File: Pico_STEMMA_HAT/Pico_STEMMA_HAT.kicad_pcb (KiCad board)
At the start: 2 copper layers, 58 x 63 mm, 38 parts, among them J1 Conn_01x20_Socket, J2 Conn_01x20_Socket

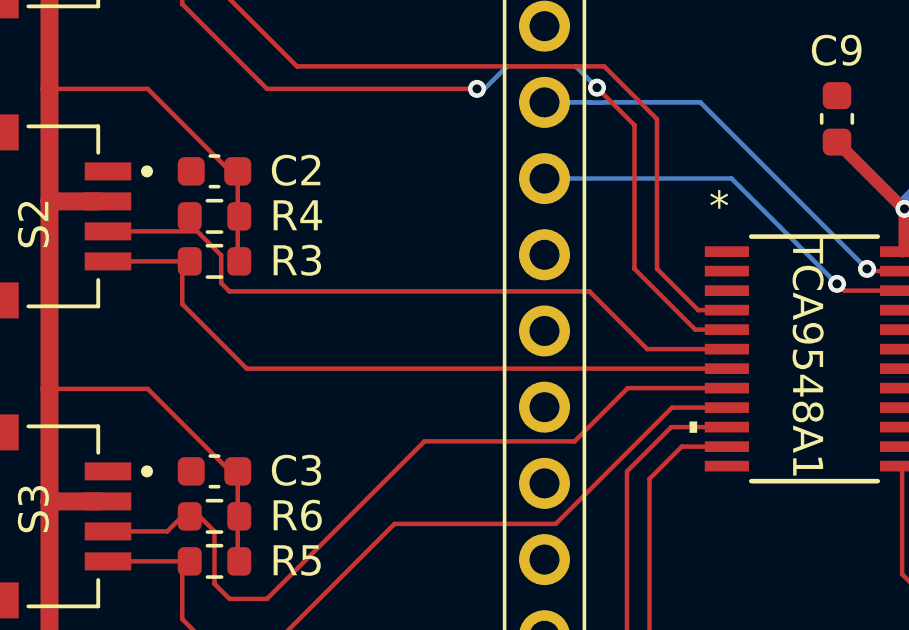
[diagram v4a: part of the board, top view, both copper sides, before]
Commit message: Reroute traces
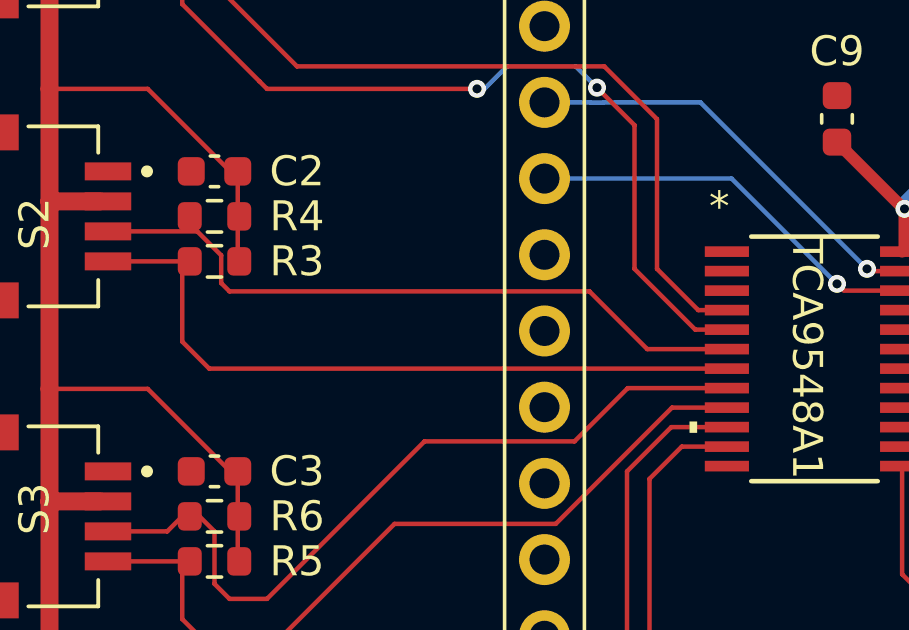
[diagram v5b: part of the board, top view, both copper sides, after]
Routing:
- net /SCL1: track 23.2 -> 23.9 mm
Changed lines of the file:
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@@
 	)
 	(segment
-		(start 131.074998 100.074998)
+		(start 128.925 99.175)
+		(end 129.824998 100.074998)
+		(width 0.15)
+		(layer "F.Cu")
+		(net 38)
+	)
+	(segment
+		(start 128.925 96.5)
+		(end 128.925 99.175)
+		(width 0.15)
+		(layer "F.Cu")
+		(net 38)
+	)
+	(segment
+		(start 129.824998 100.074998)
 		(end 147.079 100.074998)
-		(width 0.15)
-		(layer "F.Cu")
-		(net 38)
-	)
-	(segment
-		(start 128.925 96.5)
-		(end 128.925 97.925)
-		(width 0.15)
-		(layer "F.Cu")
-		(net 38)
-	)
-	(segment
-		(start 128.925 97.925)
-		(end 131.074998 100.074998)
 		(width 0.15)
 		(layer "F.Cu")
@@
 	)
 	(segment
+		(start 157.25 84.75)
+		(end 156.5 85.5)
+		(width 0.15)
+		(layer "F.Cu")
+		(net 51)
+	)
+	(segment
+		(start 156.074998 99.425002)
+		(end 152.921 99.425002)
+		(width 0.15)
+		(layer "F.Cu")
+		(net 51)
+	)
+	(segment
+		(start 174.05 84.5)
+		(end 172.75 84.5)
+		(width 0.15)
+		(layer "F.Cu")
+		(net 51)
+	)
+	(segment
+		(start 171.25 85)
+		(end 170.5 84.25)
+		(width 0.15)
+		(layer "F.Cu")
+		(net 51)
+	)
+	(segment
 		(start 156.5 85.5)
 		(end 156.5 99)
@@
 	)
 	(segment
+		(start 168.75 82)
+		(end 166 84.75)
+		(width 0.15)
+		(layer "F.Cu")
+		(net 51)
+	)
+	(segment
+		(start 170.5 82.5)
+		(end 170 82)
+		(width 0.15)
+		(layer "F.Cu")
+		(net 51)
+	)
+	(segment
+		(start 172.25 85)
+		(end 171.25 85)
+		(width 0.15)
+		(layer "F.Cu")
+		(net 51)
+	)
+	(segment
+		(start 166 84.75)
+		(end 157.25 84.75)
+		(width 0.15)
+		(layer "F.Cu")
+		(net 51)
+	)
+	(segment
+		(start 172.75 84.5)
+		(end 172.25 85)
+		(width 0.15)
+		(layer "F.Cu")
+		(net 51)
+	)
+	(segment
 		(start 170 82)
 		(end 168.75 82)
@@
 	)
 	(segment
-		(start 171.25 85)
-		(end 170.5 84.25)
-		(width 0.15)
-		(layer "F.Cu")
-		(net 51)
-	)
-	(segment
 		(start 170.5 84.25)
 		(end 170.5 82.5)
 		(width 0.15)
 		(layer "F.Cu")
-		(net 51)
-	)
-	(segment
-		(start 172.25 85)
-		(end 171.25 85)
-		(width 0.15)
-		(layer "F.Cu")
-		(net 51)
-	)
-	(segment
-		(start 172.75 84.5)
-		(end 172.25 85)
-		(width 0.15)
-		(layer "F.Cu")
-		(net 51)
-	)
-	(segment
-		(start 166 84.75)
-		(end 157.25 84.75)
-		(width 0.15)
-		(layer "F.Cu")
-		(net 51)
-	)
-	(segment
-		(start 174.05 84.5)
-		(end 172.75 84.5)
-		(width 0.15)
-		(layer "F.Cu")
-		(net 51)
-	)
-	(segment
-		(start 157.25 84.75)
-		(end 156.5 85.5)
-		(width 0.15)
-		(layer "F.Cu")
-		(net 51)
-	)
-	(segment
-		(start 170.5 82.5)
-		(end 170 82)
-		(width 0.15)
-		(layer "F.Cu")
-		(net 51)
-	)
-	(segment
-		(start 168.75 82)
-		(end 166 84.75)
-		(width 0.15)
-		(layer "F.Cu")
-		(net 51)
-	)
-	(segment
-		(start 156.074998 99.425002)
-		(end 152.921 99.425002)
-		(width 0.15)
-		(layer "F.Cu")

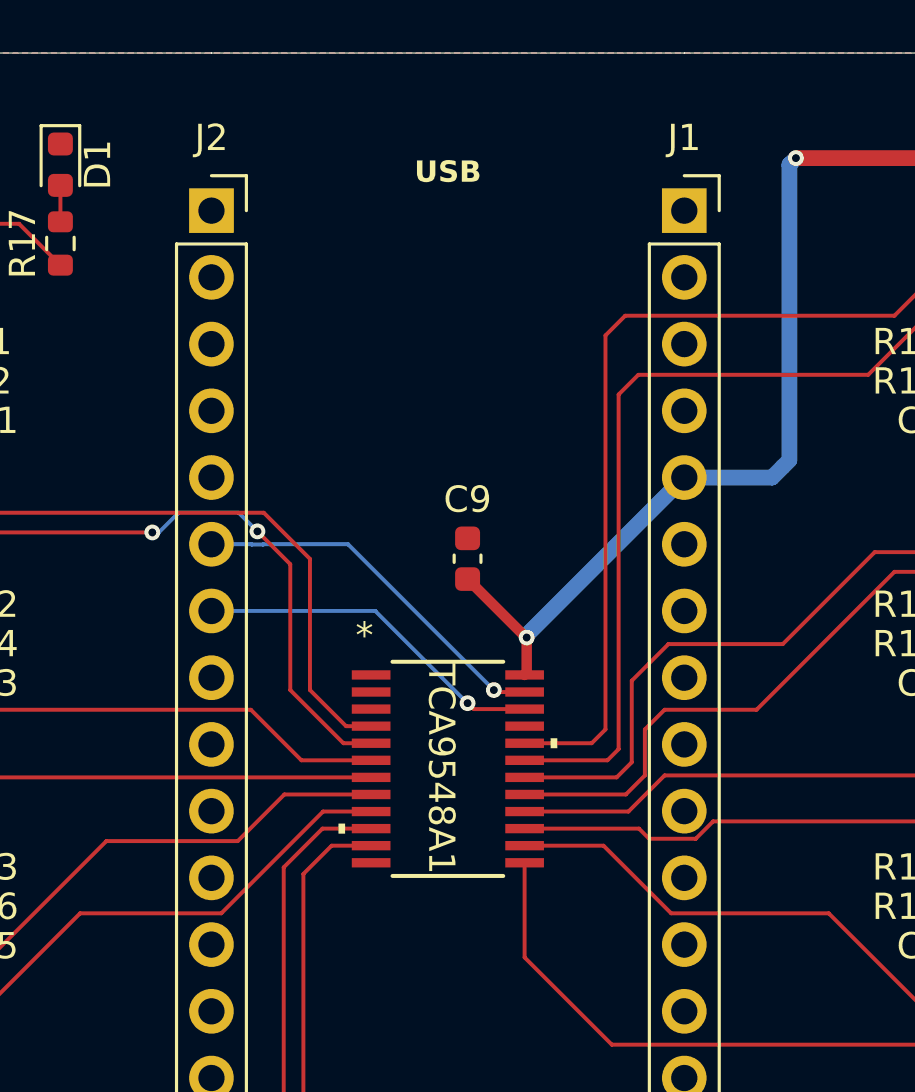
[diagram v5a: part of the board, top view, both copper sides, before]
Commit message: Add 3D models to the repo
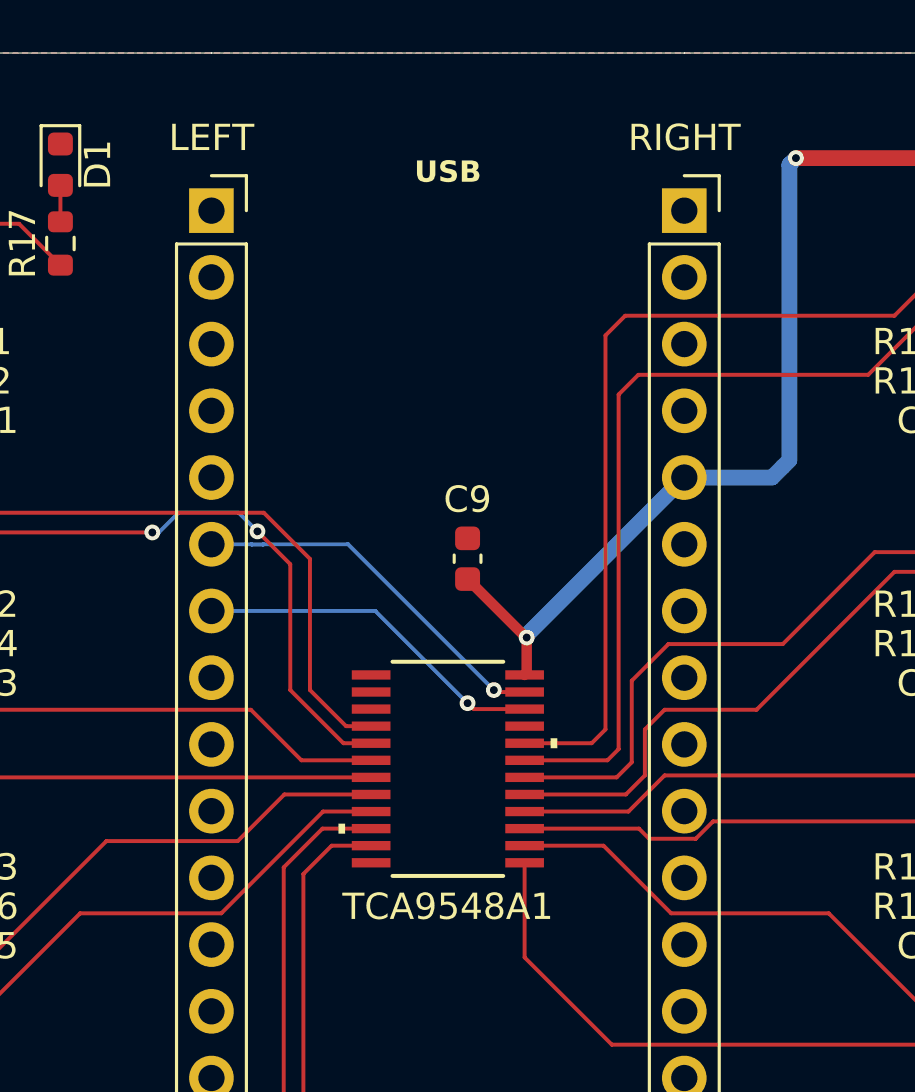
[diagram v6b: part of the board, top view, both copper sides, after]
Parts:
- renumbered J2 to LEFT, J1 to RIGHT
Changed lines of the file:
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@@
 		(descr "Through hole straight socket strip, 1x20, 2.54mm pitch, single row (from Kicad 4.0.7), script generated")
 		(tags "Through hole socket strip THT 1x20 2.54mm single row")
-		(property "Reference" "J1"
+		(property "Reference" "RIGHT"
 			(at 0 -2.77 0)
 			(layer "F.SilkS")
@@
 		(descr "Through hole straight socket strip, 1x20, 2.54mm pitch, single row (from Kicad 4.0.7), script generated")
 		(tags "Through hole socket strip THT 1x20 2.54mm single row")
-		(property "Reference" "J2"
+		(property "Reference" "LEFT"
 			(at 0 -2.77 0)
 			(layer "F.SilkS")
@@
 		(tags "TCA9548APWR ")
 		(property "Reference" "TCA9548A1"
-			(at -0.25 0 -90)
+			(at 0 5.25 0)
 			(unlocked yes)
 			(layer "F.SilkS")
@@
 			(layer "F.Fab")
 		)
-		(fp_text user "*"
-			(at -3.175 -5.0736 0)
-			(layer "F.SilkS")
-			(effects
-				(font
-					(size 1 1)
-					(thickness 0.15)
-				)
-			)
-		)
-		(fp_text user "*"
-			(at -3.175 -5.0736 0)
-			(layer "F.SilkS")
-			(effects
-				(font
-					(size 1 1)
-					(thickness 0.15)
-				)
-			)
-		)
-		(fp_text user "*"
-			(at -1.8669 -3.8735 0)
+		(fp_text user "${REFERENCE}"
+			(at 0 5.25 0)
 			(unlocked yes)
 			(layer "F.Fab")
@@
 			)
 		)
-		(fp_text user "${REFERENCE}"
-			(at 0 5.25 0)
+		(fp_text user "*"
+			(at -1.8669 -3.8735 0)
 			(unlocked yes)
 			(layer "F.Fab")

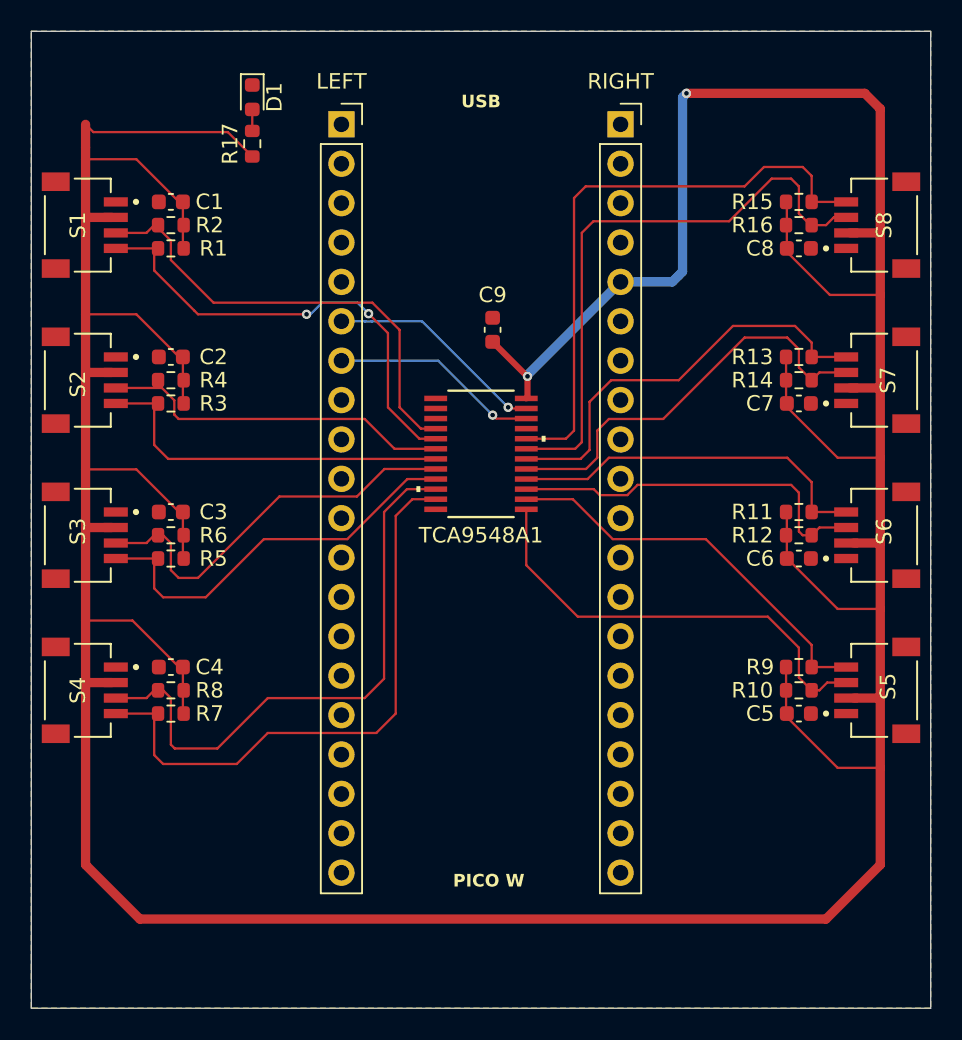
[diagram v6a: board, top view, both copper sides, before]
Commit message: Add GND vias to connect STEMMA GNDs
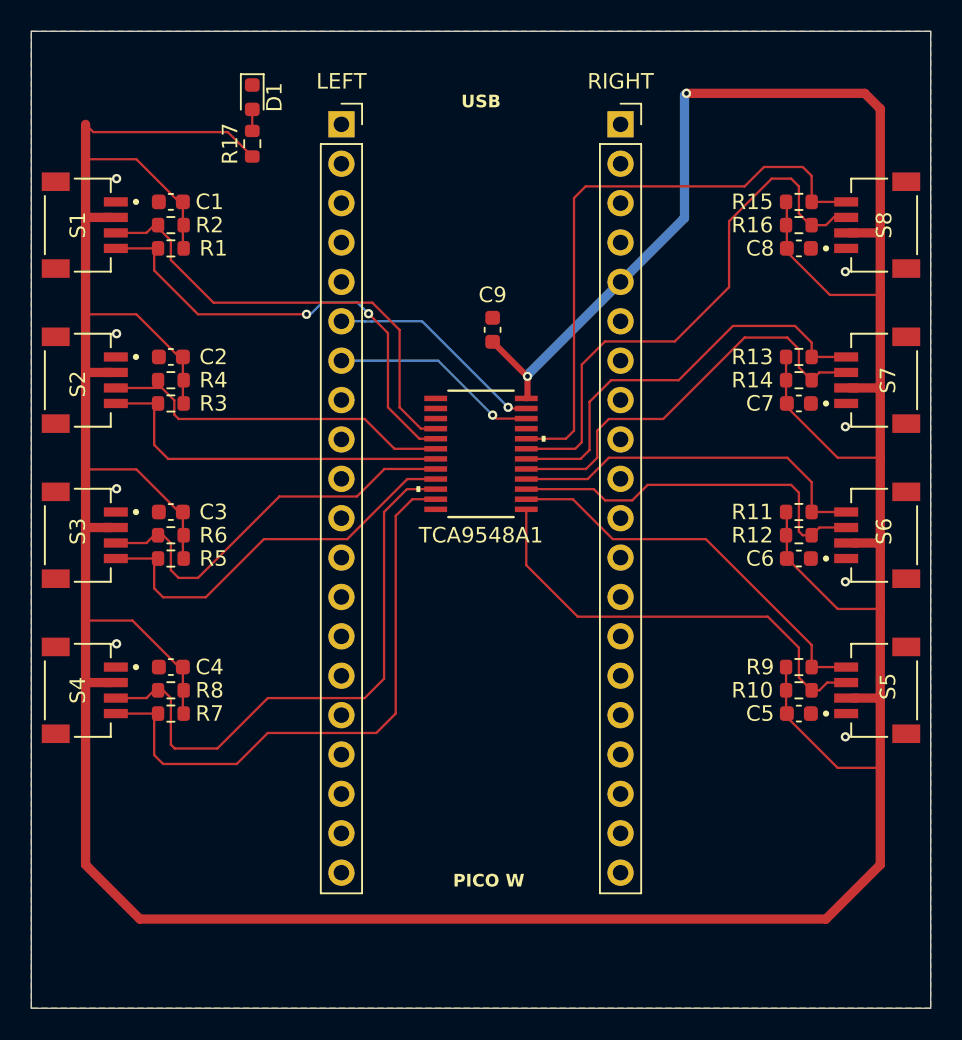
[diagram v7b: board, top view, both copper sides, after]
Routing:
- net /SDA7: track 38.7 -> 36.2 mm
- net +3V3: track 301.2 -> 299.3 mm
- net GND: vias 0 -> 8
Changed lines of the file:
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@@
 		)
+	)
+	(via
+		(at 126.5 92)
+		(size 0.6)
+		(drill 0.3)
+		(layers "F.Cu" "B.Cu")
+		(free yes)
+		(net 1)
+	)
+	(via
+		(at 173.5 108)
+		(size 0.6)
+		(drill 0.3)
+		(layers "F.Cu" "B.Cu")
+		(free yes)
+		(net 1)
+	)
+	(via
+		(at 126.5 102)
+		(size 0.6)
+		(drill 0.3)
+		(layers "F.Cu" "B.Cu")
+		(free yes)
+		(net 1)
+	)
+	(via
+		(at 173.5 88)
+		(size 0.6)
+		(drill 0.3)
+		(layers "F.Cu" "B.Cu")
+		(free yes)
+		(net 1)
+	)
+	(via
+		(at 126.5 112)
+		(size 0.6)
+		(drill 0.3)
+		(layers "F.Cu" "B.Cu")
+		(free yes)
+		(net 1)
+	)
+	(via
+		(at 173.5 98)
+		(size 0.6)
+		(drill 0.3)
+		(layers "F.Cu" "B.Cu")
+		(free yes)
+		(net 1)
+	)
+	(via
+		(at 173.5 118)
+		(size 0.6)
+		(drill 0.3)
+		(layers "F.Cu" "B.Cu")
+		(free yes)
+		(net 1)
+	)
+	(via
+		(at 126.5 82)
+		(size 0.6)
+		(drill 0.3)
+		(layers "F.Cu" "B.Cu")
+		(free yes)
+		(net 1)
 	)
 	(segment
@@
 	)
 	(segment
-		(start 162.75 88.25)
-		(end 163 88)
+		(start 159 88.66)
+		(end 153 94.66)
+		(width 0.6)
+		(layer "B.Cu")
+		(net 2)
+	)
+	(segment
+		(start 163.125 84.535)
+		(end 159 88.66)
 		(width 0.6)
 		(layer "B.Cu")
@@
 	)
 	(segment
-		(start 159 88.66)
-		(end 153 94.66)
+		(start 163.125 76.625)
+		(end 163.125 84.535)
 		(width 0.6)
 		(layer "B.Cu")
@@
 	)
 	(segment
-		(start 162.34 88.66)
-		(end 162.75 88.25)
-		(width 0.6)
-		(layer "B.Cu")
-		(net 2)
-	)
-	(segment
-		(start 159 88.66)
-		(end 162.34 88.66)
-		(width 0.6)
-		(layer "B.Cu")
-		(net 2)
-	)
-	(segment
-		(start 163 76.75)
-		(end 163.25 76.5)
-		(width 0.6)
-		(layer "B.Cu")
-		(net 2)
-	)
-	(segment
-		(start 163 88)
-		(end 163 76.75)
+		(start 163.25 76.5)
+		(end 163.125 76.625)
 		(width 0.6)
 		(layer "B.Cu")
@@
 	)
 	(segment
-		(start 170 101.75)
-		(end 160.097753 101.75)
+		(start 159.75 102.75)
+		(end 158 102.75)
 		(width 0.15)
 		(layer "F.Cu")
@@
 	)
 	(segment
-		(start 157.662 102.412)
+		(start 170.75 105)
+		(end 170.5 104.75)
+		(width 0.15)
+		(layer "F.Cu")
+		(net 47)
+	)
+	(segment
+		(start 171.825 104.5)
+		(end 171.325 105)
+		(width 0.15)
+		(layer "F.Cu")
+		(net 47)
+	)
+	(segment
+		(start 170.5 102.25)
+		(end 170 101.75)
+		(width 0.15)
+		(layer "F.Cu")
+		(net 47)
+	)
+	(segment
+		(start 173.55 104.5)
+		(end 171.825 104.5)
+		(width 0.15)
+		(layer "F.Cu")
+		(net 47)
+	)
+	(segment
+		(start 158 102.75)
 		(end 157.274999 102.024999)
+		(width 0.15)
+		(layer "F.Cu")
+		(net 47)
+	)
+	(segment
+		(start 170.5 104.75)
+		(end 170.5 102.25)
+		(width 0.15)
+		(layer "F.Cu")
+		(net 47)
+	)
+	(segment
+		(start 171.325 105)
+		(end 170.75 105)
 		(width 0.15)
 		(layer "F.Cu")
@@
 	)
 	(segment
-		(start 171.825 104.5)
-		(end 171.325 105)
+		(start 160.75 101.75)
+		(end 159.75 102.75)
 		(width 0.15)
 		(layer "F.Cu")
@@
 	)
 	(segment
-		(start 159.435753 102.412)
-		(end 157.662 102.412)
-		(width 0.15)
-		(layer "F.Cu")
-		(net 47)
-	)
-	(segment
-		(start 171.325 105)
-		(end 170.75 105)
-		(width 0.15)
-		(layer "F.Cu")
-		(net 47)
-	)
-	(segment
-		(start 173.55 104.5)
-		(end 171.825 104.5)
-		(width 0.15)
-		(layer "F.Cu")
-		(net 47)
-	)
-	(segment
-		(start 170.5 102.25)
-		(end 170 101.75)
-		(width 0.15)
-		(layer "F.Cu")
-		(net 47)
-	)
-	(segment
-		(start 170.75 105)
-		(end 170.5 104.75)
-		(width 0.15)
-		(layer "F.Cu")
-		(net 47)
-	)
-	(segment
-		(start 160.097753 101.75)
-		(end 159.435753 102.412)
-		(width 0.15)
-		(layer "F.Cu")
-		(net 47)
-	)
-	(segment
-		(start 170.5 104.75)
-		(end 170.5 102.25)
+		(start 170 101.75)
+		(end 160.75 101.75)
 		(width 0.15)
 		(layer "F.Cu")
@@
 	)
 	(segment
+		(start 170.5 82.5)
+		(end 170 82)
+		(width 0.15)
+		(layer "F.Cu")
+		(net 51)
+	)
+	(segment
+		(start 170 82)
+		(end 168.75 82)
+		(width 0.15)
+		(layer "F.Cu")
+		(net 51)
+	)
+	(segment
+		(start 162.5 92.5)
+		(end 158 92.5)
+		(width 0.15)
+		(layer "F.Cu")
+		(net 51)
+	)
+	(segment
+		(start 172.25 85)
+		(end 171.25 85)
+		(width 0.15)
+		(layer "F.Cu")
+		(net 51)
+	)
+	(segment
+		(start 170.5 84.25)
+		(end 170.5 82.5)
+		(width 0.15)
+		(layer "F.Cu")
+		(net 51)
+	)
+	(segment
+		(start 156.074998 99.425002)
+		(end 152.921 99.425002)
+		(width 0.15)
+		(layer "F.Cu")
+		(net 51)
+	)
+	(segment
+		(start 166 84.75)
+		(end 166 89)
+		(width 0.15)
+		(layer "F.Cu")
+		(net 51)
+	)
+	(segment
+		(start 156.5 94)
+		(end 156.5 99)
+		(width 0.15)
+		(layer "F.Cu")
+		(net 51)
+	)
+	(segment
+		(start 171.25 85)
+		(end 170.5 84.25)
+		(width 0.15)
+		(layer "F.Cu")
+		(net 51)
+	)
+	(segment
+		(start 172.75 84.5)
+		(end 172.25 85)
+		(width 0.15)
+		(layer "F.Cu")
+		(net 51)
+	)
+	(segment
 		(start 156.5 99)
 		(end 156.074998 99.425002)
@@
 	)
 	(segment
-		(start 157.25 84.75)
-		(end 156.5 85.5)
+		(start 168.75 82)
+		(end 166 84.75)
 		(width 0.15)
 		(layer "F.Cu")
@@
 	)
 	(segment
-		(start 156.074998 99.425002)
-		(end 152.921 99.425002)
+		(start 166 89)
+		(end 162.5 92.5)
 		(width 0.15)
 		(layer "F.Cu")
@@
 	)
 	(segment
-		(start 171.25 85)
-		(end 170.5 84.25)
-		(width 0.15)
-		(layer "F.Cu")
-		(net 51)
-	)
-	(segment
-		(start 156.5 85.5)
-		(end 156.5 99)
-		(width 0.15)
-		(layer "F.Cu")
-		(net 51)
-	)
-	(segment
-		(start 168.75 82)
-		(end 166 84.75)
-		(width 0.15)
-		(layer "F.Cu")
-		(net 51)
-	)
-	(segment
-		(start 170.5 82.5)
-		(end 170 82)
-		(width 0.15)
-		(layer "F.Cu")
-		(net 51)
-	)
-	(segment
-		(start 172.25 85)
-		(end 171.25 85)
-		(width 0.15)
-		(layer "F.Cu")
-		(net 51)
-	)
-	(segment
-		(start 166 84.75)
-		(end 157.25 84.75)
-		(width 0.15)
-		(layer "F.Cu")
-		(net 51)
-	)
-	(segment
-		(start 172.75 84.5)
-		(end 172.25 85)
-		(width 0.15)
-		(layer "F.Cu")
-		(net 51)
-	)
-	(segment
-		(start 170 82)
-		(end 168.75 82)
-		(width 0.15)
-		(layer "F.Cu")
-		(net 51)
-	)
-	(segment
-		(start 170.5 84.25)
-		(end 170.5 82.5)
-		(width 0.15)
-		(layer "F.Cu")
+		(start 158 92.5)
+		(end 156.5 94)
+		(width 0.15)
+		(layer "F.Cu")
